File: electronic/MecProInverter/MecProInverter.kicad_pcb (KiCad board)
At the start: 2 copper layers, 3 parts, among them U1 USB-TYPE-C-007, U2 ESP32-S3-MINI-1-N8, U3 IKCM20L60GA

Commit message: electronic
library expanded
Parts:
- removed U1: USB-TYPE-C-007, footprint:TYPE-C-SMD_USB-TYPE-C-007
- removed U2: ESP32-S3-MINI-1-N8, footprint:BULETM-SMD_ESP32-S3-MINI-1-N8
- removed U3: IKCM20L60GA, footprint:DIP-24_L36.0-W21.0-P1.60-LS28.6-TL
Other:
- copper layers 2 -> 4

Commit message: electronic
-power: added 15/3,3 Volt voltage regulator
- power: added power relay
- control: added USB-ISO, added User interface
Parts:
- added U2: ESP32-S3-MINI-1-N8, footprint:BULETM-SMD_ESP32-S3-MINI-1-N8, F.Cu at (140.3, 102.2)
- added U3: IKCM20L60GA, footprint:DIP-24_L36.0-W21.0-P1.60-LS28.6-TL, F.Cu at (207.1, 84.8)

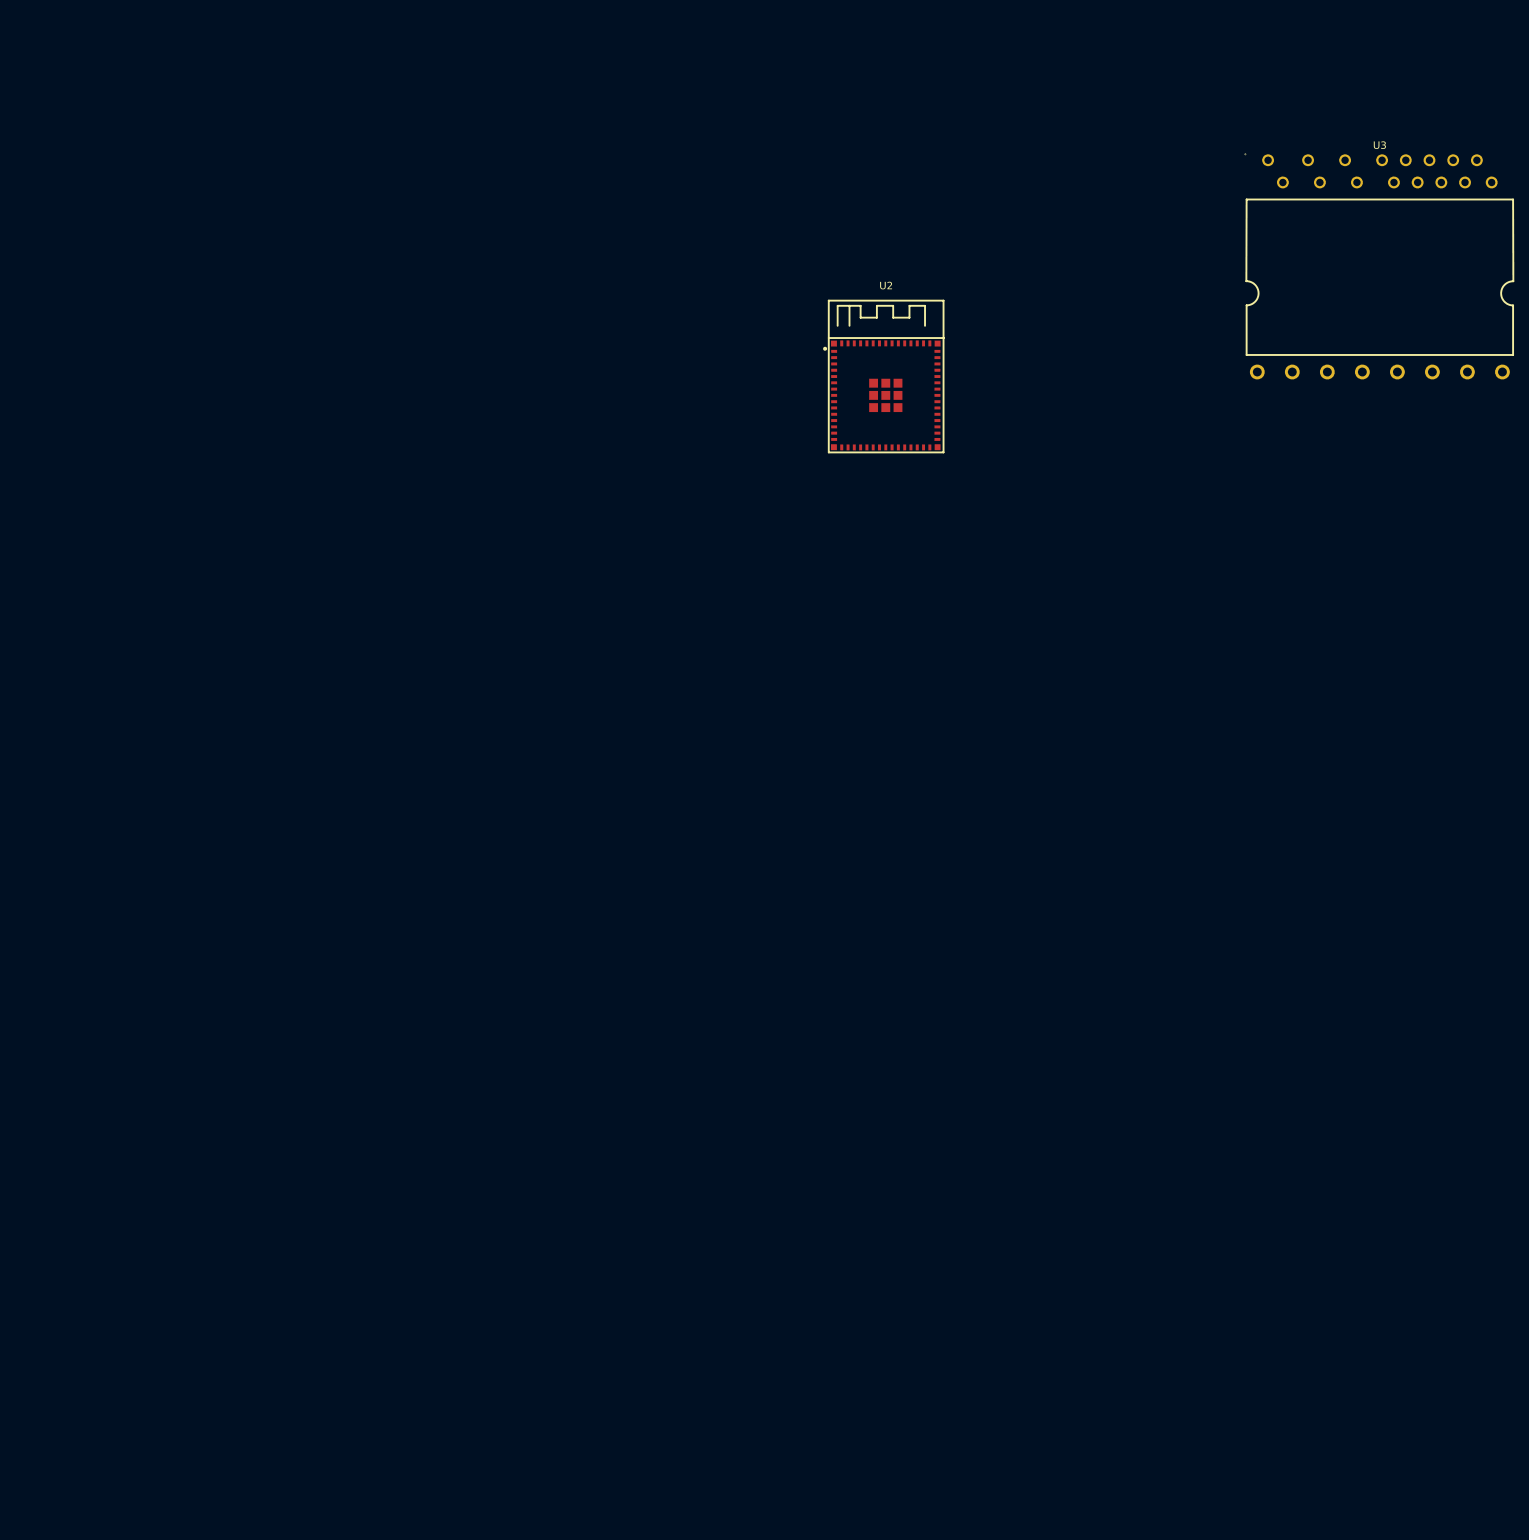
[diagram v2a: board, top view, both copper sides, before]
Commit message: electronic
Added: current sensor
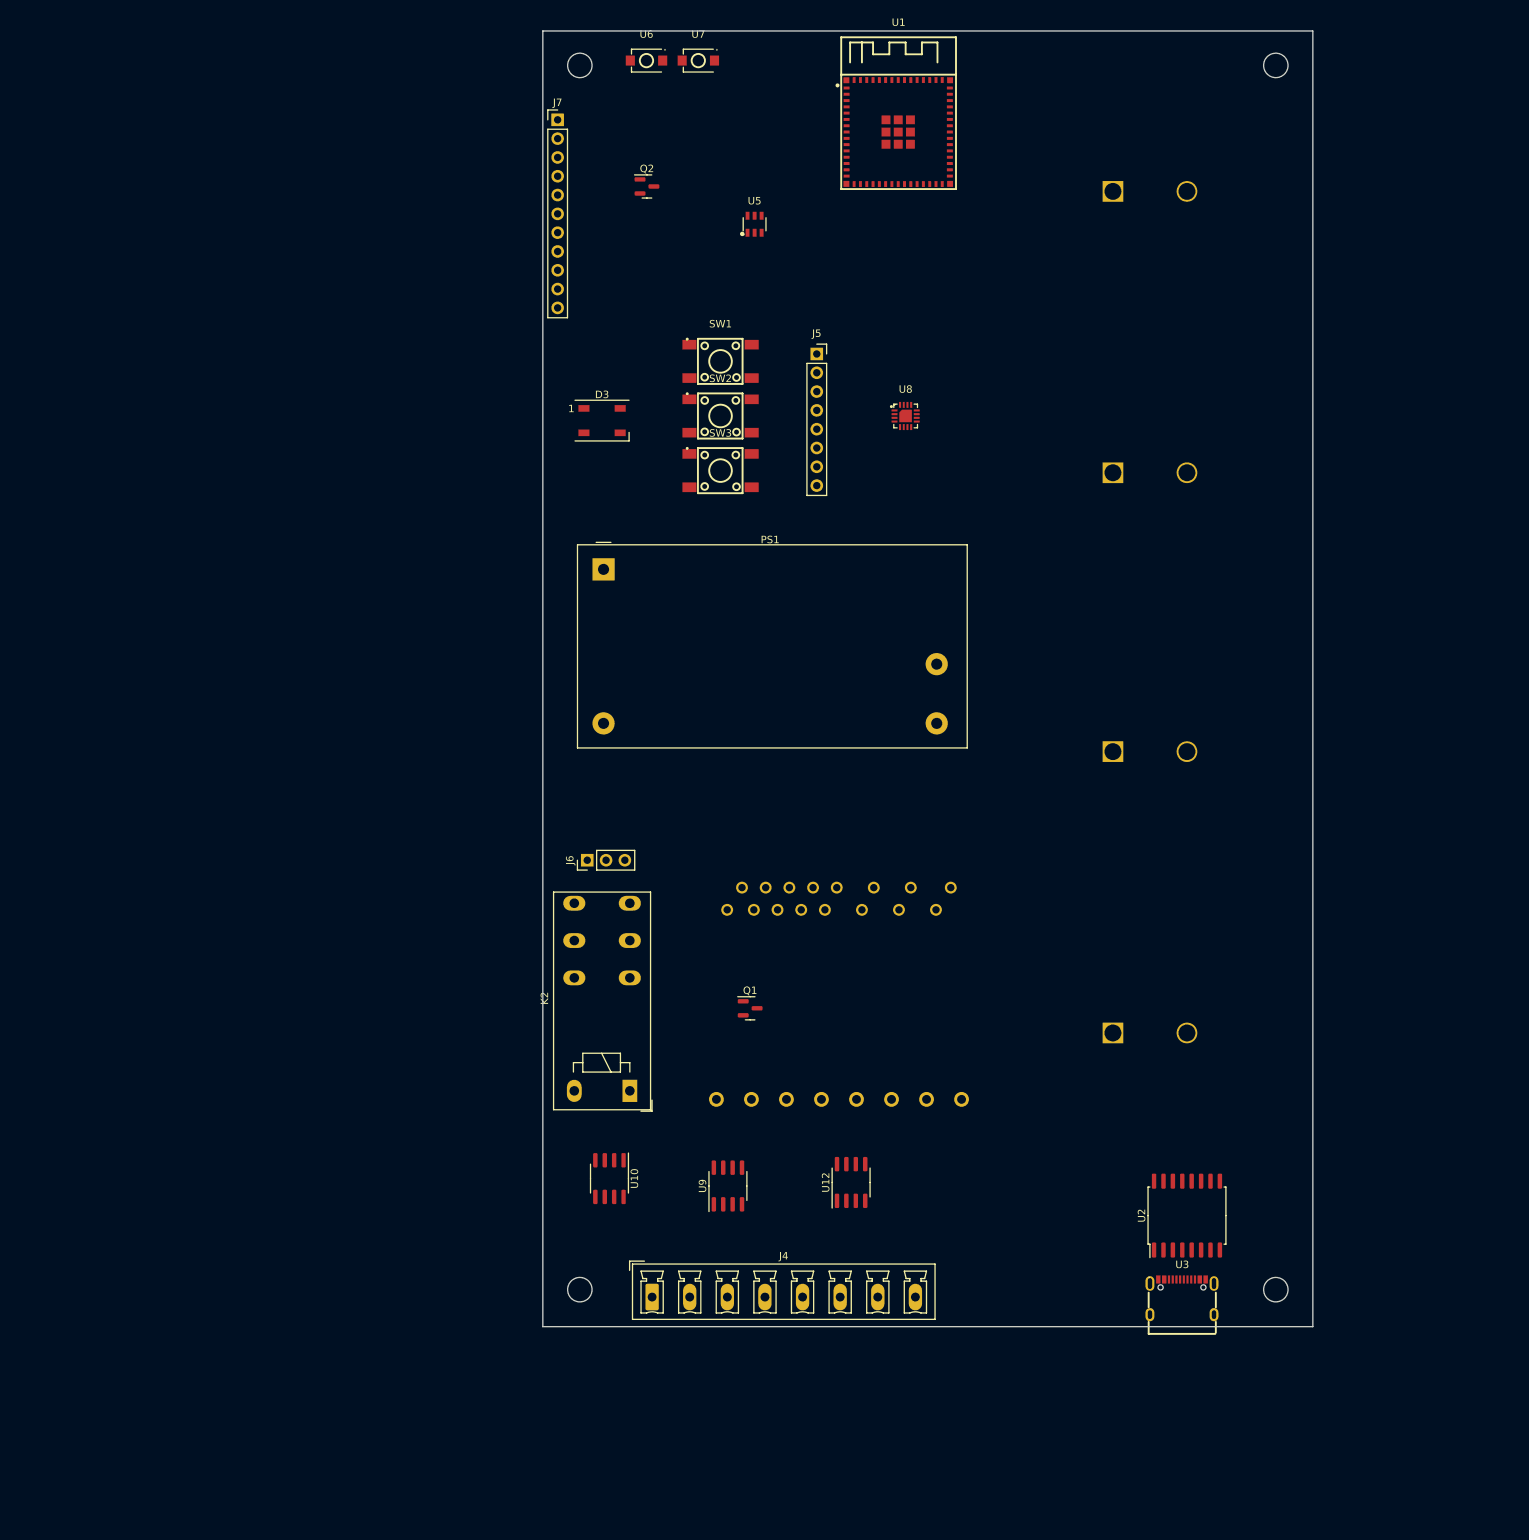
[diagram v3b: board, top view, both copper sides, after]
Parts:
- added C1: 1mF, footprints:ESMQ351VSN102MA50S, B.Cu at (171.0, 74.7)
- added C2: 1mF, footprints:ESMQ351VSN102MA50S, B.Cu at (171.0, 112.7)
- added C3: 1mF, footprints:ESMQ351VSN102MA50S, B.Cu at (171.0, 150.3)
- added C4: locked, footprints:ESMQ351VSN102MA50S, B.Cu at (171.0, 188.3)
- added D3: WS2812B, LED_SMD:LED_WS2812B_PLCC4_5.0x5.0mm_P3.2mm, F.Cu at (102.0, 105.6)
- added J4: Screw_Terminal_01x08, Connector_Phoenix_MC_HighVoltage:PhoenixContact_MCV_1,5_8-G-5.08_1x08_P5.08mm_Vertical, F.Cu at (108.8, 224.0)
- added J5: Conn_01x08, Connector_PinSocket_2.54mm:PinSocket_1x08_P2.54mm_Vertical, F.Cu at (131.0, 96.6)
- added J6: LM61, Connector_PinHeader_2.54mm:PinHeader_1x03_P2.54mm_Vertical, F.Cu at (100.0, 165.0)
- added J7: Conn_01x11, Connector_PinHeader_2.54mm:PinHeader_1x11_P2.54mm_Vertical, F.Cu at (96.0, 65.0)
- added K2: RT314A12, Relay_THT:Relay_SPDT_Schrack-RT1-16A-FormC_RM5mm, F.Cu at (105.8, 196.2)
- added PS1: IRM-20-15, Converter_ACDC:Converter_ACDC_MeanWell_IRM-20-xx_THT, F.Cu at (102.2, 125.7)
- added Q1: DMN3404L, Package_TO_SOT_SMD:SOT-23, F.Cu at (122.0, 185.0)
- added Q2: DMN3404L, Package_TO_SOT_SMD:SOT-23, F.Cu at (108.1, 74.0)
- added SW1: PTS645SM95SMTR92LFS, footprint:KEY-SMD_4P-L6.1-W6.1-P4.50-LS9.0, F.Cu at (118.0, 97.6)
- added SW2: PTS645SM95SMTR92LFS, footprint:KEY-SMD_4P-L6.1-W6.1-P4.50-LS9.0, F.Cu at (118.0, 105.0)
- added SW3: PTS645SM95SMTR92LFS, footprint:KEY-SMD_4P-L6.1-W6.1-P4.50-LS9.0, F.Cu at (118.0, 112.4)
- added U1: ESP32-S3-MINI-1-N8, footprint:BULETM-SMD_ESP32-S3-MINI-1-N8, F.Cu at (142.0, 66.7)
- added U10: ACS722xLCTR-40AB, Package_SO:SOIC-8_3.9x4.9mm_P1.27mm, F.Cu at (103.0, 208.0)
- added U12: ACS722xLCTR-40AB, Package_SO:SOIC-8_3.9x4.9mm_P1.27mm, F.Cu at (135.6, 208.5)
- added U13: IKCM20L60GA, footprint:DIP-24_L36.0-W21.0-P1.60-LS28.6-TL, B.Cu at (134.0, 183.0)
- added U5: TPS563201DDCR, footprint:SOT-23-6_L2.9-W1.6-P0.95-LS2.8-BL, F.Cu at (122.6, 79.1)
- added U6: SKRKAEE020, footprint:SW-SMD_L3.9-W3.0-P4.45, F.Cu at (108.0, 57.0)
- added U7: SKRKAEE020, footprint:SW-SMD_L3.9-W3.0-P4.45, F.Cu at (115.0, 57.0)
- added U8: TLA2528IRTER, footprint:WQFN-16_L3.0-W3.0-P0.50-TL-EP1.7, F.Cu at (143.0, 105.0)
- added U9: ACS722xLCTR-40AB, Package_SO:SOIC-8_3.9x4.9mm_P1.27mm, F.Cu at (119.0, 209.0)
- U2: value ESP32-S3-MINI-1-N8 -> ADUM3160; footprint footprint:BULETM-SMD_ESP32-S3-MINI-1-N8 -> Package_SO:SOIC-16W_7.5x10.3mm_P1.27mm
- U3: value IKCM20L60GA -> TYPE-C_16PIN_2MD(073); footprint footprint:DIP-24_L36.0-W21.0-P1.60-LS28.6-TL -> footprint:USB-C-SMD_TYPE-C-6PIN-2MD-073
- moved U3 141.8 mm to (180.3, 224.0)
- moved U2 118.0 mm to (181.0, 213.0), turned to 90 degrees
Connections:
- U2 pad 1: GND -> +5V
- U2 pad 10: unconnected-(U2-IO6-Pad10) -> /Control/USB_DP
- U2 pad 11: unconnected-(U2-IO7-Pad11) -> /Control/USB_DN
- U2 pad 12: unconnected-(U2-IO8-Pad12) -> Net-(U2-PIN)
- U2 pad 13: unconnected-(U2-IO9-Pad13) -> Net-(U2-PIN)
- U2 pad 14: unconnected-(U2-IO10-Pad14) -> Net-(U2-PIN)
- U2 pad 15: unconnected-(U2-IO11-Pad15) -> GND
- U2 pad 16: unconnected-(U2-IO12-Pad16) -> +3.3V
- U2 pad 3: +3.3V -> Net-(U2-PDEN)
- U2 pad 4: unconnected-(U2-IO0-Pad4) -> Net-(U2-PDEN)
- U2 pad 5: unconnected-(U2-IO1-Pad5) -> Net-(U2-PDEN)
- U2 pad 6: unconnected-(U2-IO2-Pad6) -> Net-(U2-UD-)
- U2 pad 7: unconnected-(U2-IO3-Pad7) -> Net-(U2-UD+)
- U2 pad 8: unconnected-(U2-IO4-Pad8) -> GND
- U2 pad 9: unconnected-(U2-IO5-Pad9) -> GND
- U3 pad 1: Net-(U3-VS(U)) -> GND
- U3 pad 10: Net-(U3-LIN(U)) -> unconnected-(U3-CC2-Pad10)
- U3 pad 11: Net-(U3-LIN(V)) -> +5V
- U3 pad 12: Net-(U3-LIN(W)) -> GND
- U3 pad 13: +15V -> GND
- U3 pad 14: unconnected-(U3-VFO-Pad14) -> GND
- U3 pad 2: Net-(U3-VB(U)) -> +5V
- U3 pad 3: Net-(U3-VS(V)) -> unconnected-(U3-SBU2-Pad3)
- U3 pad 4: Net-(U3-VB(V)) -> unconnected-(U3-CC1-Pad4)
- U3 pad 5: Net-(U3-VS(W)) -> Net-(U3-DN1)
- U3 pad 6: Net-(U3-VB(W)) -> Net-(U3-DP1)
- U3 pad 7: Net-(U3-HIN(U)) -> Net-(U3-DN1)
- U3 pad 8: Net-(U3-HIN(V)) -> Net-(U3-DP1)
- U3 pad 9: Net-(U3-HIN(W)) -> unconnected-(U3-SBU1-Pad9)
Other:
- board outline added: 104 x 175 mm

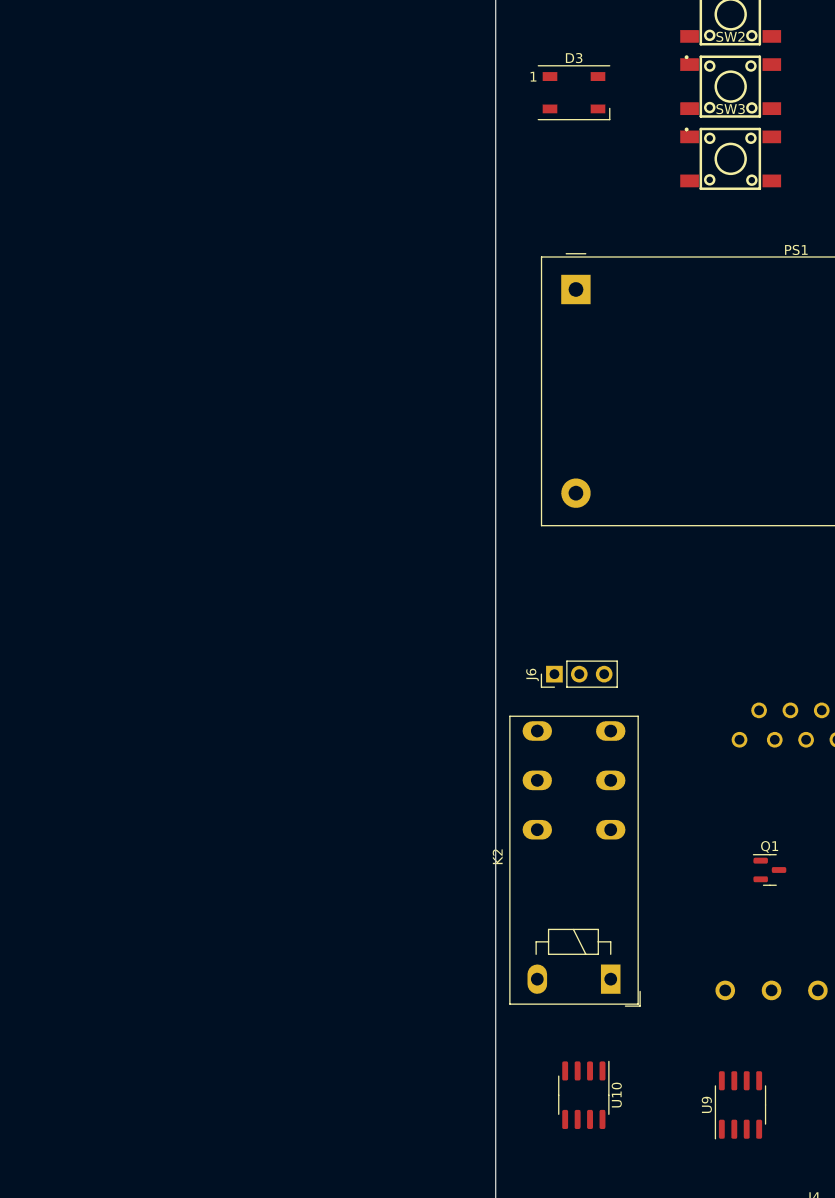
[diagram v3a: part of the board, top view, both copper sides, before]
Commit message: Electronic
Rework: Fan, ESP32 Pinout, 15V Power,
Added: GPIO ISO, ESD
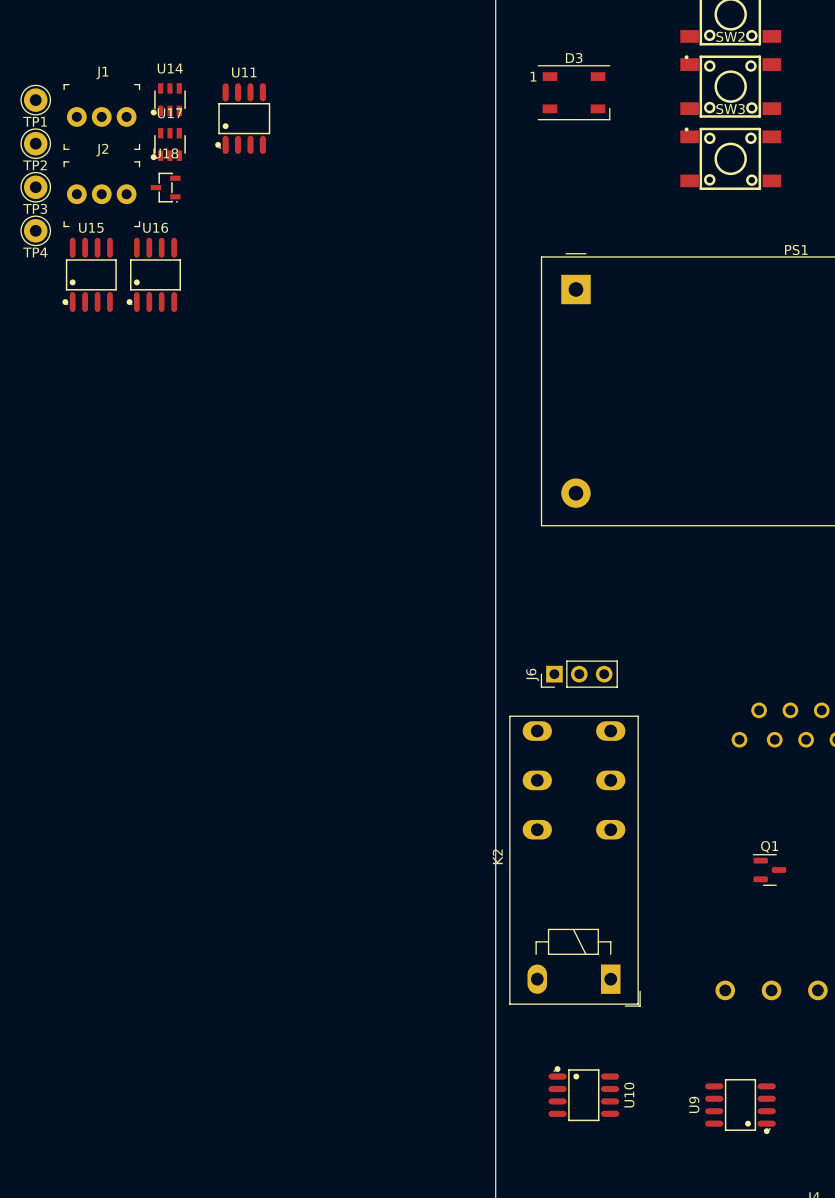
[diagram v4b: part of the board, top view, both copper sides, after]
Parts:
- added J1: 0022232031, digikey-footprints:PinHeader_1x3_P2.54mm_Drill1.02mm, F.Cu at (51.2, 108.1)
- added J2: 0022232031, digikey-footprints:PinHeader_1x3_P2.54mm_Drill1.02mm, F.Cu at (51.2, 116.0)
- added TP1: TestPoint, Connector_Pin:Pin_D1.0mm_L10.0mm_LooseFit, F.Cu at (47.0, 106.4)
- added TP2: TestPoint, Connector_Pin:Pin_D1.0mm_L10.0mm_LooseFit, F.Cu at (47.0, 110.8)
- added TP3: TestPoint, Connector_Pin:Pin_D1.0mm_L10.0mm_LooseFit, F.Cu at (47.0, 115.3)
- added TP4: TestPoint, Connector_Pin:Pin_D1.0mm_L10.0mm_LooseFit, F.Cu at (47.0, 119.7)
- added U11: CC6904SO-30A, footprint:SOP-8_L4.9-W3.9-P1.27-LS6.0-BL, F.Cu at (68.3, 108.3)
- added U14: PSRV05-4MR6T1G, footprint:SOT-23-6_L2.9-W1.6-P0.95-LS2.8-BL, F.Cu at (60.7, 106.3)
- added U15: ADUM1201ARZ-RL7, footprint:SOIC-8_L4.9-W3.9-P1.27-LS6.0-BL, F.Cu at (52.7, 124.2)
- added U16: ADUM1201ARZ-RL7, footprint:SOIC-8_L4.9-W3.9-P1.27-LS6.0-BL, F.Cu at (59.3, 124.2)
- added U17: PSRV05-4MR6T1G, footprint:SOT-23-6_L2.9-W1.6-P0.95-LS2.8-BL, F.Cu at (60.7, 110.9)
- added U18: PMV100EPAR, footprint:SOT-23-3_L2.9-W1.3-P1.90-LS2.3-BR, F.Cu at (60.3, 115.3)
- U10, U9: value ACS722xLCTR-40AB -> CC6904SO-30A; footprint Package_SO:SOIC-8_3.9x4.9mm_P1.27mm -> footprint:SOP-8_L4.9-W3.9-P1.27-LS6.0-BL
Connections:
- net +5V renamed +5VD
- J4 pad 2: GND -> /Power/AC_N
- J5 pad 3: unconnected-(J5-Pin_3-Pad3) -> Net-(J5-Pin_3)
- J5 pad 4: unconnected-(J5-Pin_4-Pad4) -> Net-(J5-Pin_4)
- J5 pad 5: unconnected-(J5-Pin_5-Pad5) -> Net-(J5-Pin_5)
- J5 pad 6: unconnected-(J5-Pin_6-Pad6) -> Net-(J5-Pin_6)
- PS1 pad 2: GND -> /Power/AC_N
- U10 pad 1: Net-(K2-Pad14) -> Net-(U13-U)
- U10 pad 2: Net-(K2-Pad14) -> Net-(U13-U)
- U10 pad 3: Net-(U4-~Phase) -> /Power/U
- U10 pad 4: Net-(U4-~Phase) -> /Power/U
- U10 pad 6: GND -> unconnected-(U10-NC-Pad6)
- U10 pad 7: /Power/CURRENT_AC -> Net-(U10-OUT)
- U2 pad 2: GND -> GNDD
- U2 pad 8: GND -> GNDD
- U3 pad 1: GND -> GNDD
- U3 pad 12: GND -> GNDD
- U3 pad 13: GND -> GNDD
- U3 pad 14: GND -> GNDD
- U5 pad 1: unconnected-(U5-GND-Pad1) -> GND
- U8 pad 2: Net-(U12-VIOUT) -> Net-(U8-AIN3/GPIO3)
- U9 pad 1: Net-(U13-W) -> Net-(K2-Pad14)
- U9 pad 2: Net-(U13-W) -> Net-(K2-Pad14)
- U9 pad 3: /Power/W -> Net-(U4-~Phase)
- U9 pad 4: /Power/W -> Net-(U4-~Phase)
- U9 pad 6: GND -> unconnected-(U9-NC-Pad6)
- U9 pad 7: Net-(U8-AIN4/GPIO4) -> Net-(U9-OUT)
